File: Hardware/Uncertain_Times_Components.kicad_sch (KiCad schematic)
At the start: 82 parts, among them J1 Conn_01x12_Male, J2 Conn_01x12_Male, J3 Conn_01x16_Male, J4 Conn_01x16_Male, J5 SWD_Header, J6 Eurorack_16_pin_power, J7 UART_Test_Pins, J8 USB_B_Micro, Q1 MMBT3904, Q2 MMBT3904, U1 STM32G473V, U2 STF202-22T1G, U3 TL074, U4 TL074, U5 LT1117-3.3, Y1 8MHz 20pF

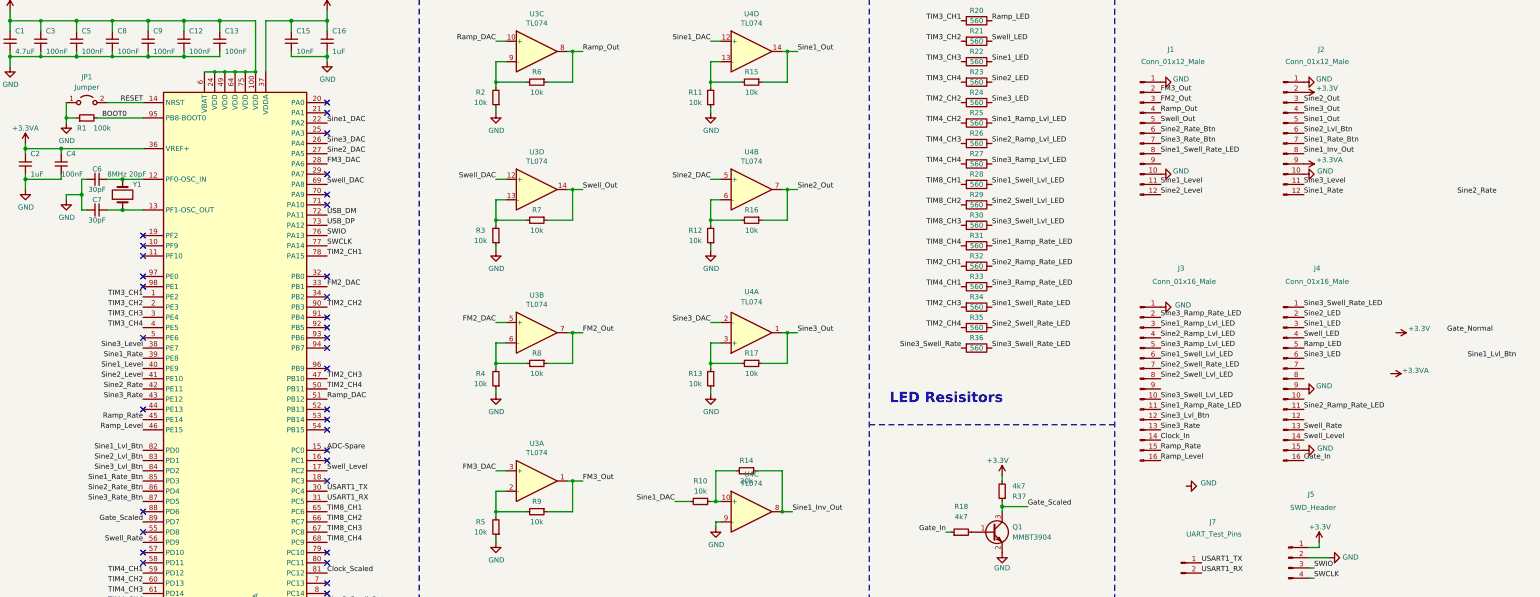
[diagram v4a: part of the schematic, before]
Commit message: Signal Routing done
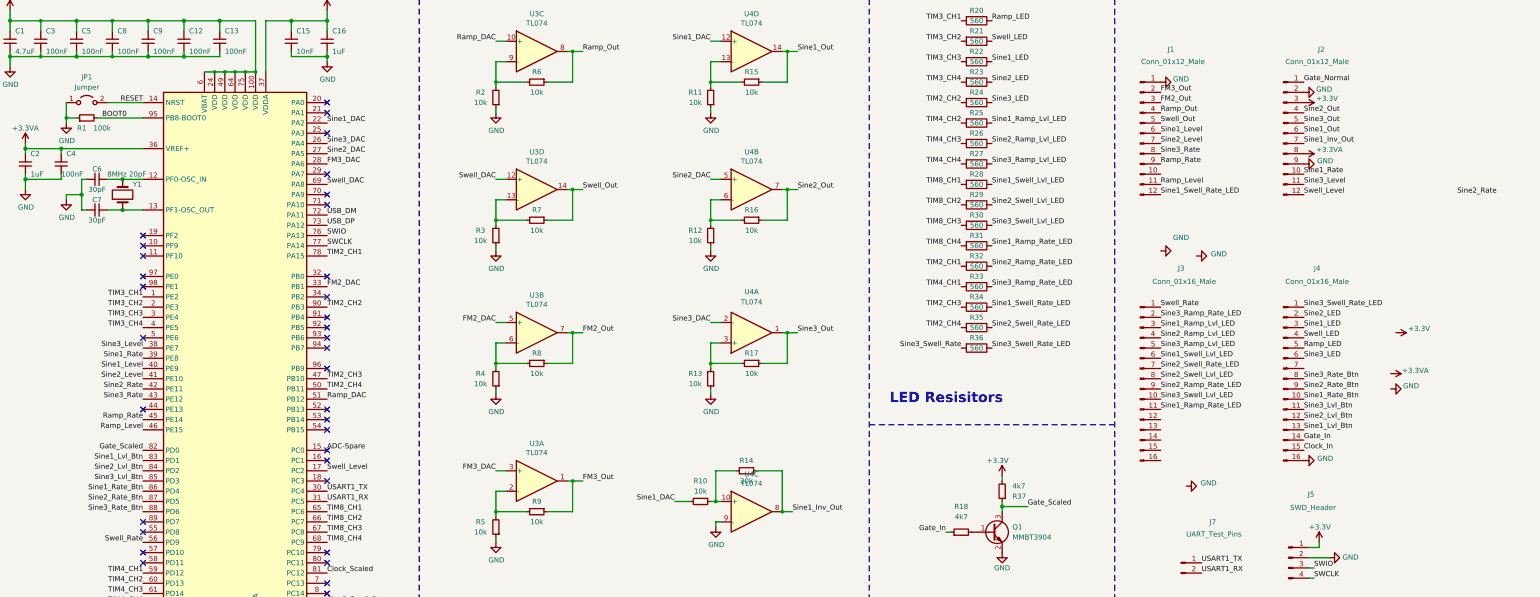
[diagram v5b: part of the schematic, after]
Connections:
- net +3.3V: now also J2.3 (Pin_3); no longer J2.2 (Pin_2)
- net +3.3VA: now also J2.8 (Pin_8); no longer J2.9 (Pin_9)
- net Clock_In: now also J4.15 (Pin_15); no longer J3.14 (Pin_14)
- net GND: now also J2.2 (Pin_2), J2.9 (Pin_9), J4.16 (Pin_16); no longer J1.10 (Pin_10), J2.1 (Pin_1), J2.10 (Pin_10), J3.1 (Pin_1), J4.15 (Pin_15), J4.9 (Pin_9)
- net Gate_In: now also J4.14 (Pin_14); no longer J4.16 (Pin_16)
- net Gate_Normal: now also J2.1 (Pin_1)
- net Gate_Scaled: now also U1.82 (PD0); no longer U1.89 (PD7)
- net Ramp_Level: now also J1.11 (Pin_11); no longer J3.16 (Pin_16)
- net Ramp_Rate: now also J1.9 (Pin_9); no longer J3.15 (Pin_15)
- net Sine1_Inv_Out: now also J2.7 (Pin_7); no longer J2.8 (Pin_8)
- net Sine1_Level: now also J1.6 (Pin_6); no longer J1.11 (Pin_11)
- net Sine1_Lvl_Btn: now also J4.13 (Pin_13), U1.83 (PD1); no longer U1.82 (PD0)
- net Sine1_Out: now also J2.6 (Pin_6); no longer J2.5 (Pin_5)
- net Sine1_Rate: now also J2.10 (Pin_10); no longer J2.12 (Pin_12)
- net Sine1_Rate_Btn: now also J4.10 (Pin_10), U1.86 (PD4); no longer J2.7 (Pin_7), U1.85 (PD3)
- net Sine1_Swell_Rate_LED: now also J1.12 (Pin_12); no longer J1.8 (Pin_8)
- net Sine2_Level: now also J1.7 (Pin_7); no longer J1.12 (Pin_12)
- net Sine2_Lvl_Btn: now also J4.12 (Pin_12), U1.84 (PD2); no longer J2.6 (Pin_6), U1.83 (PD1)
- net Sine2_Out: now also J2.4 (Pin_4); no longer J2.3 (Pin_3)
- net Sine2_Ramp_Rate_LED: now also J3.9 (Pin_9); no longer J4.11 (Pin_11)
- net Sine2_Rate_Btn: now also J4.9 (Pin_9), U1.87 (PD5); no longer J1.6 (Pin_6), U1.86 (PD4)
- net Sine3_Lvl_Btn: now also J4.11 (Pin_11), U1.85 (PD3); no longer J3.12 (Pin_12), U1.84 (PD2)
- net Sine3_Out: now also J2.5 (Pin_5); no longer J2.4 (Pin_4)
- net Sine3_Rate: now also J1.8 (Pin_8); no longer J3.13 (Pin_13)
- net Sine3_Rate_Btn: now also J4.8 (Pin_8), U1.88 (PD6); no longer J1.7 (Pin_7), U1.87 (PD5)
- net Swell_Level: now also J2.12 (Pin_12); no longer J4.14 (Pin_14)
- net Swell_Rate: now also J3.1 (Pin_1); no longer J4.13 (Pin_13)
